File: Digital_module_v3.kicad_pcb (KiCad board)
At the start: 4 copper layers, 58.3 x 67.8 mm, 2 parts, among them J1 Pow_mng_iface, J7 Pow_mng_pow

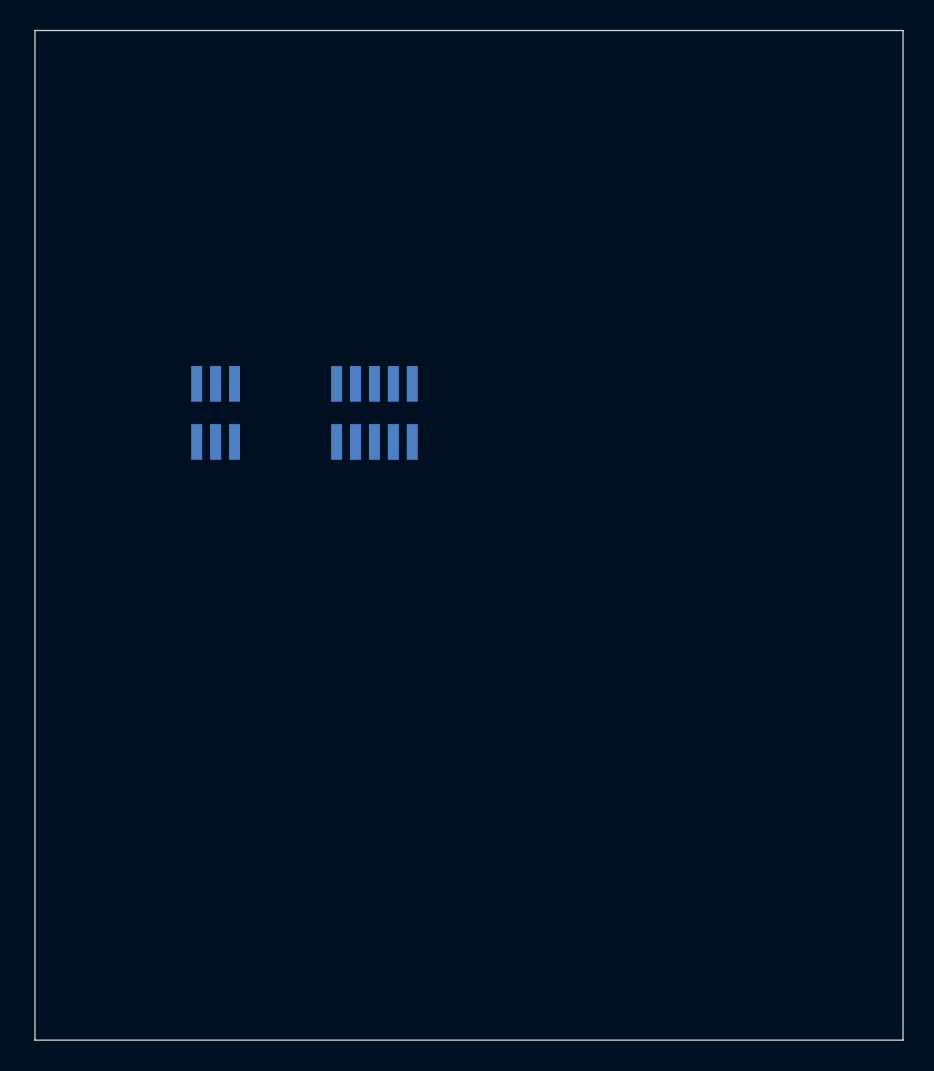
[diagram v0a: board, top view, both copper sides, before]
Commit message: Завершена трассировка печатной платы. Исправлены ошибки в схема.
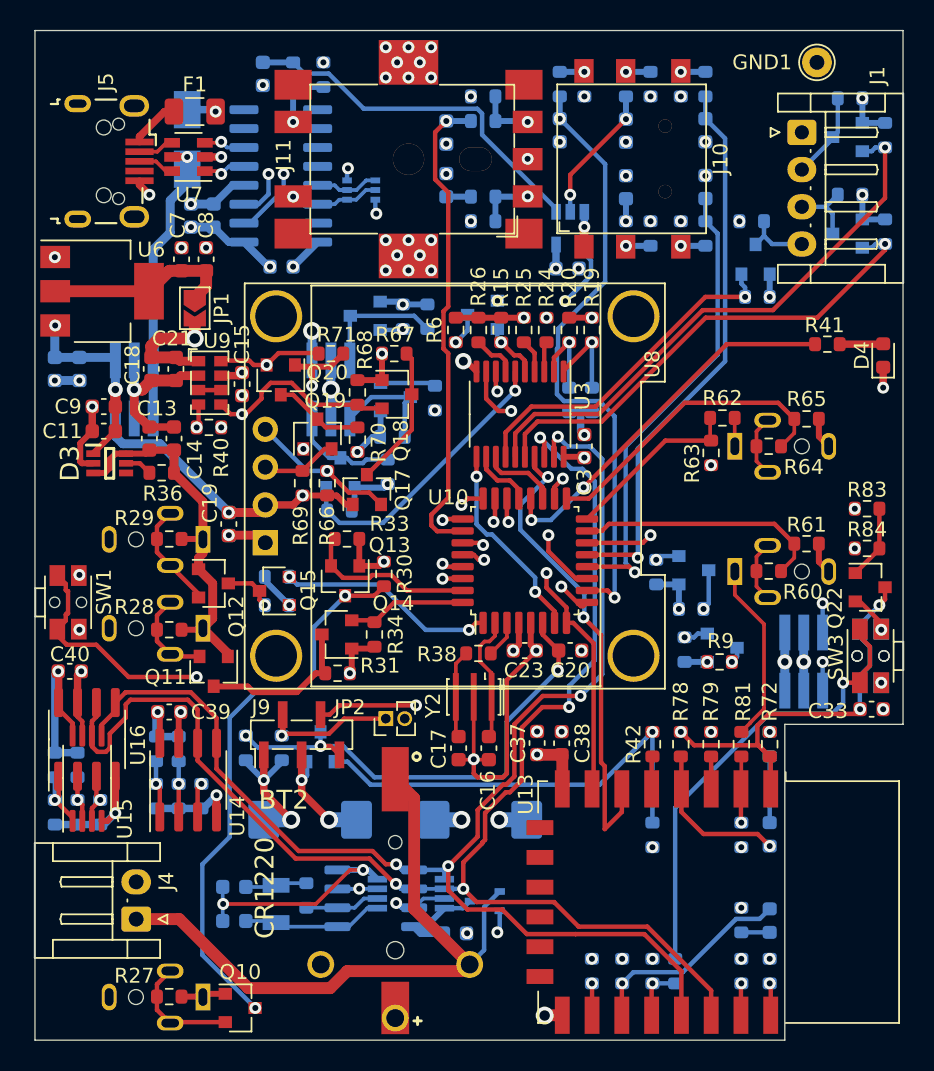
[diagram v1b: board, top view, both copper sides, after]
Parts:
- added BT1: CR2032, Modules:CR2032BS51, B.Cu at (100.0, 137.7)
- added BT2: CR1220, Modules:CR1220HSMD, F.Cu at (95.0, 133.0)
- added C1: 10pF, Capacitor_SMD:C_0603_1608Metric, B.Cu at (84.2, 134.8)
- added C10: 470uF, Capacitor_Tantalum_SMD:CP_EIA-7343-31_Kemet-D, B.Cu at (89.3, 128.0)
- added C11: 100nF, Capacitor_SMD:C_0603_1608Metric, F.Cu at (75.5, 101.9)
- added C12: 470uF, Capacitor_Tantalum_SMD:CP_EIA-7343-31_Kemet-D, B.Cu at (100.8, 128.0)
- added C13: 100nF, Capacitor_SMD:C_0603_1608Metric, F.Cu at (78.5, 102.4)
- added C14: 10uF, Capacitor_SMD:C_0603_1608Metric, F.Cu at (80.2, 102.4)
- added C15: 2.2uF, Capacitor_SMD:C_0603_1608Metric, F.Cu at (84.8, 98.7)
- added C16: 10pF, Capacitor_SMD:C_0603_1608Metric, F.Cu at (101.3, 123.2)
- added C17: 10pF, Capacitor_SMD:C_0603_1608Metric, F.Cu at (99.3, 123.2)
- added C18: 1.0uF, Capacitor_SMD:C_0603_1608Metric, F.Cu at (78.7, 97.7)
- added C19: 100nF, Capacitor_SMD:C_0603_1608Metric, F.Cu at (83.9, 108.1)
- added C2: 10pF, Capacitor_SMD:C_0603_1608Metric, B.Cu at (84.2, 132.5)
- added C20: 100nF, Capacitor_SMD:C_0603_1608Metric, F.Cu at (106.8, 116.6)
- added C21: 0.1uF, Capacitor_SMD:C_0603_1608Metric, F.Cu at (80.3, 97.7)
- added C22: 10uF, Capacitor_SMD:C_0603_1608Metric, B.Cu at (83.9, 108.1)
- added C23: 100nF, Capacitor_SMD:C_0603_1608Metric, F.Cu at (103.7, 116.6)
- added C24: 100nF, Capacitor_SMD:C_0603_1608Metric, B.Cu at (115.9, 85.5)
- added C25: 100nF, Capacitor_SMD:C_0603_1608Metric, B.Cu at (110.5, 81.7)
- added C26: 100nF, Capacitor_SMD:C_0603_1608Metric, B.Cu at (115.9, 81.7)
- added C27: 100nF, Capacitor_SMD:C_0603_1608Metric, B.Cu at (106.1, 81.7)
- added C28: 100nF, Capacitor_SMD:C_0603_1608Metric, B.Cu at (110.5, 85.5)
- added C29: 100nF, Capacitor_SMD:C_0603_1608Metric, B.Cu at (106.6, 91.0)
- added C3: 100nF, Capacitor_SMD:C_0603_1608Metric, F.Cu at (107.7, 102.9)
- added C30: 100nF, Capacitor_SMD:C_0603_1608Metric, B.Cu at (98.5, 85.4)
- added C31: 100nF, Capacitor_SMD:C_0603_1608Metric, B.Cu at (98.5, 81.9)
- added C32: 100nF, Capacitor_SMD:C_0603_1608Metric, B.Cu at (86.2, 77.9)
- added C33: 100nF, Capacitor_SMD:C_0603_1608Metric, F.Cu at (127.0, 120.6)
- added C34: 100nF, Capacitor_SMD:C_0603_1608Metric, B.Cu at (82.9, 87.4)
- added C35: 10uF, Capacitor_SMD:C_0603_1608Metric, B.Cu at (81.3, 87.4)
- added C36: 100nF, Capacitor_SMD:C_0603_1608Metric, B.Cu at (87.4, 90.9)
- added C37: 10uF, Capacitor_SMD:C_0603_1608Metric, F.Cu at (104.6, 122.8)
- added C38: 100nF, Capacitor_SMD:C_0603_1608Metric, F.Cu at (106.2, 122.9)
- added C39: 100nF, Capacitor_SMD:C_0603_1608Metric, F.Cu at (79.9, 120.8)
- added C4: 100nF, Capacitor_SMD:C_0603_1608Metric, B.Cu at (99.1, 135.6)
- added C40: 100nF, Capacitor_SMD:C_0603_1608Metric, F.Cu at (73.2, 118.0)
- added C5: 10uF, Capacitor_SMD:C_0603_1608Metric, B.Cu at (73.8, 97.7)
- added C6: 100nF, Capacitor_SMD:C_0603_1608Metric, B.Cu at (72.2, 97.7)
- added C7: 100nF, Capacitor_SMD:C_0603_1608Metric, F.Cu at (80.7, 90.4)
- added C8: 10uF, Capacitor_SMD:C_0603_1608Metric, F.Cu at (82.3, 90.4)
- added C9: 10uF, Capacitor_SMD:C_0603_1608Metric, F.Cu at (75.5, 100.3)
- added D1: BAT54CW, Package_TO_SOT_SMD:SOT-323_SC-70, B.Cu at (101.1, 133.5)
- added D2: SS14, Diode_SMD:D_SMA, B.Cu at (81.1, 82.3)
- added D3: LM66100DCKR, Modules:SOP65P210X110-6N, F.Cu at (75.9, 104.1)
- added D4: LED, LED_SMD:LED_0603_1608Metric, F.Cu at (127.8, 96.8)
- added D5: LED, LED_SMD:LED_0603_1608Metric, B.Cu at (120.2, 129.0)
- added D6: LED, LED_SMD:LED_0603_1608Metric, B.Cu at (120.2, 134.8)
- added F1: 0.5A, Fuse:Fuse_1206_3216Metric, F.Cu at (81.6, 80.4)
- added GND1: GND1, TestPoint:TestPoint_THTPad_D2.0mm_Drill1.0mm, F.Cu at (123.4, 77.1)
- added J10: JoystickSwitch, Modules:JoystickSwitch, F.Cu at (110.9, 83.6)
- added J11: JoystickSwitch, Modules:EC11_SMD, F.Cu at (95.9, 83.6)
- added J2: AUB-33, Modules:AUB-33, B.Cu at (122.4, 111.3)
- added J3: AUB-33, Modules:AUB-33, B.Cu at (122.4, 102.9)
- added J4: B2B-EH-A, Connector_JST:JST_EH_S2B-EH_1x02_P2.50mm_Horizontal, F.Cu at (77.6, 134.7)
- added J5: USB_B_Micro, Modules:USB_Micro-B_Wuerth_629105150521, F.Cu at (75.7, 83.8)
- added J6: AUB-33, Modules:AUB-33, B.Cu at (77.6, 139.9)
- added J8: AUB-33, Modules:AUB-33, B.Cu at (77.6, 109.2)
- added J9: SWD(PLS5), Connector_PinSocket_1.27mm:PinSocket_1x05_P1.27mm_Vertical_SMD_Pin1Left, F.Cu at (88.8, 122.3)
- added JP1: 3V3_en, Jumper:SolderJumper-2_P1.3mm_Open_TrianglePad1.0x1.5mm, F.Cu at (81.6, 93.6)
- added JP2: BOOT0, Connector_PinHeader_1.27mm:PinHeader_1x02_P1.27mm_Vertical, F.Cu at (94.4, 121.2)
- added Q1: BSS138, Package_TO_SOT_SMD:SOT-23, B.Cu at (125.4, 82.2)
- added Q10: BSS138, Package_TO_SOT_SMD:SOT-23, F.Cu at (84.6, 140.6)
- added Q11: BSS138, Package_TO_SOT_SMD:SOT-23, F.Cu at (82.9, 118.0)
- added Q12: BSS138, Package_TO_SOT_SMD:SOT-23, F.Cu at (82.8, 112.1)
- added Q13: BSS138, Package_TO_SOT_SMD:SOT-23, F.Cu at (91.7, 112.0)
- added Q14: BSS138, Package_TO_SOT_SMD:SOT-23, F.Cu at (91.1, 115.6)
- added Q15: BSS138, Package_TO_SOT_SMD:SOT-23, F.Cu at (86.9, 112.6)
- added Q16: 2N5551S, Package_TO_SOT_SMD:SOT-23, B.Cu at (90.0, 123.1)
- added Q17: BSS138, Package_TO_SOT_SMD:SOT-23, F.Cu at (93.1, 105.8)
- added Q18: BSS138, Package_TO_SOT_SMD:SOT-23, F.Cu at (95.2, 99.4)
- added Q19: BSS138, Package_TO_SOT_SMD:SOT-23, F.Cu at (89.8, 102.1)
- added Q2: BSS138, Package_TO_SOT_SMD:SOT-23, B.Cu at (125.4, 88.6)
- added Q20: BSS138, Package_TO_SOT_SMD:SOT-23, F.Cu at (87.4, 98.5)
- added Q21: UMH3N, Package_TO_SOT_SMD:SOT-363_SC-70-6, B.Cu at (92.8, 85.7)
- added Q22: 2N5551S, Package_TO_SOT_SMD:SOT-23, F.Cu at (126.9, 112.4)
- added Q3: BSS138, Package_TO_SOT_SMD:SOT-23, B.Cu at (119.2, 90.4)
- added Q4: BSS138, Package_TO_SOT_SMD:SOT-23, B.Cu at (95.1, 99.6)
- added Q5: BSS138, Package_TO_SOT_SMD:SOT-23, B.Cu at (91.4, 104.7)
- added Q6: BSS138, Package_TO_SOT_SMD:SOT-23, B.Cu at (100.9, 94.1)
- added Q7: BSS138, Package_TO_SOT_SMD:SOT-23, B.Cu at (93.0, 94.2)
- added Q8: BSS138, Package_TO_SOT_SMD:SOT-23, B.Cu at (115.1, 111.2)
- added Q9: BSS138, Package_TO_SOT_SMD:SOT-23, B.Cu at (117.0, 116.4)
- added R1: 10G, Resistor_SMD:R_0603_1608Metric, B.Cu at (125.6, 79.6)
- added R10: 10k, Resistor_SMD:R_0603_1608Metric, B.Cu at (127.9, 82.0)
- added R11: 10k, Resistor_SMD:R_0603_1608Metric, B.Cu at (127.9, 88.5)
- added R12: 10k, Resistor_SMD:R_0603_1608Metric, B.Cu at (119.4, 92.9)
- added R13: 10k, Resistor_SMD:R_0603_1608Metric, B.Cu at (97.7, 99.7)
- added R14: 10k, Resistor_SMD:R_0603_1608Metric, B.Cu at (91.3, 107.2)
- added R15: 10k, Resistor_SMD:R_0603_1608Metric, F.Cu at (102.2, 95.1)
- added R16: 10k, Resistor_SMD:R_0603_1608Metric, B.Cu at (95.6, 94.2)
- added R17: 10k, Resistor_SMD:R_0603_1608Metric, B.Cu at (112.6, 111.4)
- added R18: 10k, Resistor_SMD:R_0603_1608Metric, B.Cu at (114.5, 116.6)
- added R19: 10k, Resistor_SMD:R_0603_1608Metric, F.Cu at (108.3, 95.1)
- added R2: 10G, Resistor_SMD:R_0603_1608Metric, B.Cu at (125.6, 86.0)
- added R20: 10k, Resistor_SMD:R_0603_1608Metric, F.Cu at (106.7, 95.1)
- added R21: 10k, Resistor_SMD:R_0603_1608Metric, B.Cu at (108.3, 99.8)
- added R22: 10k, Resistor_SMD:R_0603_1608Metric, B.Cu at (106.7, 99.8)
- added R23: 50, Resistor_SMD:R_0603_1608Metric, B.Cu at (89.1, 133.1)
- added R24: 10k, Resistor_SMD:R_0603_1608Metric, F.Cu at (105.2, 95.1)
- added R25: 10k, Resistor_SMD:R_0603_1608Metric, F.Cu at (103.7, 95.1)
- added R26: 10k, Resistor_SMD:R_0603_1608Metric, F.Cu at (100.6, 95.1)
- added R27: 10k, Resistor_SMD:R_0603_1608Metric, F.Cu at (79.9, 139.9)
- added R28: 10k, Resistor_SMD:R_0603_1608Metric, F.Cu at (79.9, 115.2)
- added R29: 10k, Resistor_SMD:R_0603_1608Metric, F.Cu at (79.9, 109.1)
- added R3: 10G, Resistor_SMD:R_0603_1608Metric, B.Cu at (119.0, 87.8)
- added R30: 10G, Resistor_SMD:R_0603_1608Metric, F.Cu at (94.3, 111.5)
- added R31: 10G, Resistor_SMD:R_0603_1608Metric, F.Cu at (91.2, 118.2)
- added R32: 10G, Resistor_SMD:R_0603_1608Metric, B.Cu at (87.1, 113.6)
- added R33: 10k, Resistor_SMD:R_0603_1608Metric, F.Cu at (91.8, 109.1)
- added R34: 10k, Resistor_SMD:R_0603_1608Metric, F.Cu at (93.6, 115.6)
- added R35: 10k, Resistor_SMD:R_0603_1608Metric, B.Cu at (87.1, 111.7)
- added R36: 10k, Resistor_SMD:R_0603_1608Metric, F.Cu at (79.4, 104.7)
- added R37: 10k, Resistor_SMD:R_0603_1608Metric, B.Cu at (87.4, 123.2)
- added R38: 50, Resistor_SMD:R_0603_1608Metric, F.Cu at (100.6, 116.8)
- added R39: 10k, Resistor_SMD:R_0603_1608Metric, B.Cu at (85.0, 123.2)
- added R4: 2.2M, Resistor_SMD:R_0603_1608Metric, B.Cu at (94.9, 102.3)
- added R40: 10k, Resistor_SMD:R_0603_1608Metric, F.Cu at (82.5, 101.7)
- added R41: 1k, Resistor_SMD:R_0603_1608Metric, F.Cu at (124.1, 96.1)
- added R42: 10k, Resistor_SMD:R_0603_1608Metric, F.Cu at (112.3, 122.9)
- added R43: 10k, Resistor_SMD:R_0603_1608Metric, B.Cu at (112.3, 129.0)
- added R44: 100k, Resistor_SMD:R_0603_1608Metric, B.Cu at (114.2, 88.6)
- added R45: 100k, Resistor_SMD:R_0603_1608Metric, B.Cu at (112.2, 78.6)
- added R46: 100k, Resistor_SMD:R_0603_1608Metric, B.Cu at (114.2, 78.6)
- added R47: 100k, Resistor_SMD:R_0603_1608Metric, B.Cu at (107.7, 78.6)
- added R48: 100k, Resistor_SMD:R_0603_1608Metric, B.Cu at (112.2, 88.6)
- added R49: 10k, Resistor_SMD:R_0603_1608Metric, B.Cu at (115.9, 88.6)
- added R5: 2.2M, Resistor_SMD:R_0603_1608Metric, B.Cu at (94.5, 104.6)
- added R50: 10k, Resistor_SMD:R_0603_1608Metric, B.Cu at (110.5, 78.6)
- added R51: 10k, Resistor_SMD:R_0603_1608Metric, B.Cu at (115.9, 78.6)
- added R52: 10k, Resistor_SMD:R_0603_1608Metric, B.Cu at (106.1, 78.6)
- added R53: 10k, Resistor_SMD:R_0603_1608Metric, B.Cu at (110.5, 88.6)
- added R54: 100k, Resistor_SMD:R_0603_1608Metric, B.Cu at (101.0, 87.8)
- added R55: 100k, Resistor_SMD:R_0603_1608Metric, B.Cu at (101.0, 79.4)
- added R56: 100k, Resistor_SMD:R_0603_1608Metric, B.Cu at (90.2, 78.0)
- added R57: 10k, Resistor_SMD:R_0603_1608Metric, B.Cu at (101.0, 86.2)
- added R58: 10k, Resistor_SMD:R_0603_1608Metric, B.Cu at (101.0, 81.1)
- added R59: 10k, Resistor_SMD:R_0603_1608Metric, B.Cu at (88.2, 78.0)
- added R6: 2.2M, Resistor_SMD:R_0603_1608Metric, F.Cu at (99.1, 95.1)
- added R60: 220k, Resistor_SMD:R_0603_1608Metric, F.Cu at (120.1, 111.3)
- added R61: 100k, Resistor_SMD:R_0603_1608Metric, F.Cu at (122.7, 109.5)
- added R62: 220k, Resistor_SMD:R_0603_1608Metric, F.Cu at (117.0, 101.0)
- added R63: 100k, Resistor_SMD:R_0603_1608Metric, F.Cu at (116.3, 103.4)
- added R64: 220k, Resistor_SMD:R_0603_1608Metric, F.Cu at (120.1, 102.9)
- added R65: 100k, Resistor_SMD:R_0603_1608Metric, F.Cu at (122.7, 101.1)
- added R66: 10k, Resistor_SMD:R_0603_1608Metric, F.Cu at (90.5, 105.4)
- added R67: 1M, Resistor_SMD:R_0603_1608Metric, F.Cu at (95.0, 96.7)
- added R68: 10k, Resistor_SMD:R_0603_1608Metric, F.Cu at (92.5, 99.3)
- added R69: 10k, Resistor_SMD:R_0603_1608Metric, F.Cu at (88.8, 105.4)
- added R7: 2.2M, Resistor_SMD:R_0603_1608Metric, B.Cu at (97.2, 94.2)
- added R70: 1M, Resistor_SMD:R_0603_1608Metric, F.Cu at (92.5, 102.5)
- added R71: 10k, Resistor_SMD:R_0603_1608Metric, F.Cu at (90.7, 96.7)
- added R72: 10k, Resistor_SMD:R_0603_1608Metric, F.Cu at (120.2, 122.9)
- added R73: 1k, Resistor_SMD:R_0603_1608Metric, B.Cu at (120.2, 122.9)
- added R74: 10k, Resistor_SMD:R_0603_1608Metric, B.Cu at (112.3, 138.2)
- added R75: 10k, Resistor_SMD:R_0603_1608Metric, B.Cu at (110.3, 138.2)
- added R76: 1k, Resistor_SMD:R_0603_1608Metric, B.Cu at (118.3, 134.7)
- added R77: 470, Resistor_SMD:R_0603_1608Metric, B.Cu at (113.8, 138.2)
- added R78: 470, Resistor_SMD:R_0603_1608Metric, F.Cu at (114.2, 122.9)
- added R79: 10k, Resistor_SMD:R_0603_1608Metric, F.Cu at (116.3, 122.9)
- added R8: 10G, Resistor_SMD:R_0603_1608Metric, B.Cu at (114.9, 113.8)
- added R80: 10k, Resistor_SMD:R_0603_1608Metric, B.Cu at (108.3, 138.2)
- added R81: 220k, Resistor_SMD:R_0603_1608Metric, F.Cu at (118.3, 122.9)
- added R82: 100k, Resistor_SMD:R_0603_1608Metric, B.Cu at (118.3, 129.0)
- added R83: 10k, Resistor_SMD:R_0603_1608Metric, F.Cu at (126.7, 107.1)
- added R84: 10k, Resistor_SMD:R_0603_1608Metric, F.Cu at (126.7, 109.8)
- added R85: 470, Resistor_SMD:R_0603_1608Metric, B.Cu at (118.3, 138.2)
- added R86: 470, Resistor_SMD:R_0603_1608Metric, B.Cu at (120.2, 138.2)
- added R87: 10k, Resistor_SMD:R_0603_1608Metric, B.Cu at (72.2, 124.3)
- added R88: 10k, Resistor_SMD:R_0603_1608Metric, B.Cu at (73.7, 124.3)
- added R89: 10k, Resistor_SMD:R_0603_1608Metric, B.Cu at (79.0, 123.2)
- added R9: 10G, Resistor_SMD:R_0603_1608Metric, F.Cu at (116.8, 117.4)
- added R90: 10k, Resistor_SMD:R_0603_1608Metric, B.Cu at (80.5, 123.2)
- added R91: 10k, Resistor_SMD:R_0603_1608Metric, B.Cu at (72.2, 127.5)
- added R92: 10k, Resistor_SMD:R_0603_1608Metric, B.Cu at (73.7, 127.5)
- added R93: 10k, Resistor_SMD:R_0603_1608Metric, B.Cu at (79.0, 126.4)
- added R94: 10k, Resistor_SMD:R_0603_1608Metric, B.Cu at (80.5, 126.4)
- added R95: 10k, Resistor_SMD:R_0603_1608Metric, B.Cu at (82.0, 126.4)
- added R96: 10k, Resistor_SMD:R_0603_1608Metric, B.Cu at (75.2, 127.5)
- added SW1: SW_Rst, Modules:SW_SPST_EVQP7C, F.Cu at (73.1, 113.4)
- added SW2: SW_RST, Modules:SW_SPST_EVQP7C, B.Cu at (127.0, 117.0)
- added SW3: SW_FLASH, Modules:SW_SPST_EVQP7C, F.Cu at (127.0, 117.0)
- added U1: Power_manager_2_v3_wo3D, Modules:Power_manager_2_v3_wo3D, B.Cu at (100.0, 96.0)
- added U10: STM32G030K6Tx, Package_QFP:LQFP-32_7x7mm_P0.8mm, F.Cu at (103.7, 110.6)
- added U11: SN74LVC1G08DBVR, Package_TO_SOT_SMD:SOT-23-5, B.Cu at (106.8, 88.3)
- added U12: CH340C, Package_SO:SOIC-16_3.9x9.9mm_P1.27mm, B.Cu at (87.4, 84.8)
- added U13: ESP-12F, RF_Module:ESP-12E, F.Cu at (116.8, 133.5)
- added U14: FM24C64B, Package_SO:SOIC-8_3.9x4.9mm_P1.27mm, F.Cu at (81.1, 125.3)
- added U15: AT24CS64-XHM, Package_SO:TSSOP-8_4.4x3mm_P0.65mm, F.Cu at (74.4, 125.2)
- added U16: AT24CS64-SSHM, Package_SO:SOIC-8_3.9x4.9mm_P1.27mm, F.Cu at (74.3, 122.6)
- added U2: Fan_control_module_2_v3, Modules:Fan_controller_2_v3_wo3D, B.Cu at (100.0, 120.5)
- added U3: PCA9544APW, Package_SO:TSSOP-20_4.4x6.5mm_P0.65mm, F.Cu at (103.4, 100.8)
- added U4: PCF8563TS, Modules:SOT65P490X110-8N, B.Cu at (96.1, 133.0)
- added U5: PCF8563TS, Package_SO:SO-8_3.9x4.9mm_P1.27mm, B.Cu at (93.7, 133.3)
- added U6: LM1117-3.3, Package_TO_SOT_SMD:SOT-223-3_TabPin2, F.Cu at (75.4, 92.5)
- added U7: USBLC6-2SC6, Package_TO_SOT_SMD:SOT-23-6, F.Cu at (81.2, 83.5)
- added U8: SSD1306, Modules:SSD1306_2_I2C, F.Cu at (86.3, 109.4)
- added U9: AP3216C, Modules:AP3216C, F.Cu at (81.8, 97.2)
- added Y1: SC-32S 32.768KHz, Crystal:Crystal_SMD_3215-2Pin_3.2x1.5mm, B.Cu at (87.0, 133.7)
- added Y2: CSTCE8M, Crystal:Resonator_SMD_muRata_CSTxExxV-3Pin_3.0x1.1mm_HandSoldering, F.Cu at (100.3, 119.7)
- J1: value Pow_mng_iface -> B2B-EH-A; footprint Connector_PinHeader_1.27mm:PinHeader_2x05_P1.27mm_Vertical_SMD -> Connector_JST:JST_EH_S4B-EH_1x04_P2.50mm_Horizontal; moved to F.Cu
- J7: value Pow_mng_pow -> AUB-33; footprint Connector_PinHeader_1.27mm:PinHeader_2x03_P1.27mm_Vertical_SMD -> Modules:AUB-33
- moved J1 34.3 mm to (122.4, 81.8), turned to 270 degrees
- moved J7 15.4 mm to (77.6, 115.1), turned to 0 degrees
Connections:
- J1 pad 2: GND1 -> /sda1
- J1 pad 3: /+5V_st -> /scl1
- J1 pad 4: /+5V_st -> Net-(J1-Pad4)
- J7 pad 1: +5VP -> +5VD
- J7 pad 2: +5VP -> GND1
- J7 pad 3: GND1 -> Net-(J7-Pad3)
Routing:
- net GND1: track 0.00 -> 122.4 mm, vias 0 -> 57
- net +3V3: track 0.00 -> 107.8 mm, vias 0 -> 47
- net /I2C_SCL: track 0.00 -> 97.6 mm, vias 0 -> 4
- net /I2C_SDA: track 0.00 -> 93.7 mm, vias 0 -> 4
- net +5P: track 0.00 -> 82.1 mm, vias 0 -> 6
- net Net-(R86-Pad2): track 0.00 -> 79.1 mm, vias 0 -> 2
- net Net-(R85-Pad2): track 0.00 -> 77.9 mm, vias 0 -> 2
- net /ESP32_part/~RST: track 0.00 -> 73.1 mm, vias 0 -> 4
- net /ESP32_part/GPIO0: track 0.00 -> 67.7 mm, vias 0 -> 2
- net +5VD: track 0.00 -> 54.7 mm
- net /Ctrl_part/~RST: track 0.00 -> 54.1 mm, vias 0 -> 4
- net /ESP_LED: track 0.00 -> 48.0 mm, vias 0 -> 2
- net Net-(BT1-Pad1): track 0.00 -> 45.2 mm
- net /Ctrl_part/jlline: track 0.00 -> 41.3 mm, vias 0 -> 2
- net /Ctrl_part/jcline: track 0.00 -> 41.2 mm, vias 0 -> 3
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- added copper zone on In1.Cu, net +3V3
- added copper zone on In2.Cu, net GND1
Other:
- outline, holes or cut-outs redrawn

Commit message: Добавлен BOM-файл в HTML-формате, гербера и файлы сверловки
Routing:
- net Net-(R86-Pad2): track 79.1 -> 83.1 mm
- net Net-(R85-Pad2): track 77.9 -> 81.9 mm
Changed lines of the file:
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@@
     (thickness 1.6)
     (drawings 33)
-    (tracks 1413)
+    (tracks 1420)
     (zones 0)
     (modules 202)
@@
       (effects (font (size 1 1) (thickness 0.15)) (justify mirror))
     )
-    (fp_text user %R (at 0 -10.16 -180) (layer B.Fab)
-      (effects (font (size 1 1) (thickness 0.15)) (justify mirror))
-    )
     (fp_line (start 21.082 -4.572) (end 20.447 -3.937) (layer B.Fab) (width 0.1))
     (fp_line (start 20.447 -1.651) (end 20.447 -3.937) (layer B.Fab) (width 0.1))
@@
     (fp_line (start 20.32 -6.35) (end 20.32 -1.6) (layer B.CrtYd) (width 0.12))
     (fp_line (start 25 -6.35) (end 20.32 -6.35) (layer B.CrtYd) (width 0.12))
+    (fp_text user %R (at 0 -10.16 -180) (layer B.Fab)
+      (effects (font (size 1 1) (thickness 0.15)) (justify mirror))
+    )
     (pad 2.3 smd rect (at 22.479 -5.05) (size 0.74 2.4) (layers B.Cu B.Paste B.Mask)
       (net 1 GND1))
@@
       (effects (font (size 1 1) (thickness 0.15)) (justify mirror))
     )
-    (pad 2 smd roundrect (at 3.1125 0) (size 2.075 2.55) (layers B.Cu B.Paste B.Mask) (roundrect_rratio 0.120482)
+    (pad 2 smd roundrect (at 3.1125 0) (size 2.075 2.55) (layers B.Cu B.Paste B.Mask) (roundrect_rratio 0.1204819277108434)
       (net 1 GND1))
-    (pad 1 smd roundrect (at -3.1125 0) (size 2.075 2.55) (layers B.Cu B.Paste B.Mask) (roundrect_rratio 0.120482)
+    (pad 1 smd roundrect (at -3.1125 0) (size 2.075 2.55) (layers B.Cu B.Paste B.Mask) (roundrect_rratio 0.1204819277108434)
       (net 5 +3V3))
     (model ${KISYS3DMOD}/Capacitor_Tantalum_SMD.3dshapes/CP_EIA-7343-31_Kemet-D.wrl
@@
       (effects (font (size 1 1) (thickness 0.15)) (justify mirror))
     )
-    (pad 2 smd roundrect (at 3.1125 0 180) (size 2.075 2.55) (layers B.Cu B.Paste B.Mask) (roundrect_rratio 0.120482)
+    (pad 2 smd roundrect (at 3.1125 0 180) (size 2.075 2.55) (layers B.Cu B.Paste B.Mask) (roundrect_rratio 0.1204819277108434)
       (net 1 GND1))
-    (pad 1 smd roundrect (at -3.1125 0 180) (size 2.075 2.55) (layers B.Cu B.Paste B.Mask) (roundrect_rratio 0.120482)
+    (pad 1 smd roundrect (at -3.1125 0 180) (size 2.075 2.55) (layers B.Cu B.Paste B.Mask) (roundrect_rratio 0.1204819277108434)
       (net 5 +3V3))
     (model ${KISYS3DMOD}/Capacitor_Tantalum_SMD.3dshapes/CP_EIA-7343-31_Kemet-D.wrl
@@
     (pad 2 thru_hole oval (at 2.5 0 270) (size 1.7 1.95) (drill 0.95) (layers *.Cu *.Mask)
       (net 55 /sda1))
-    (pad 1 thru_hole roundrect (at 0 0 270) (size 1.7 1.95) (drill 0.95) (layers *.Cu *.Mask) (roundrect_rratio 0.147059)
+    (pad 1 thru_hole roundrect (at 0 0 270) (size 1.7 1.95) (drill 0.95) (layers *.Cu *.Mask) (roundrect_rratio 0.1470588235294118)
       (net 1 GND1))
     (model ${KISYS3DMOD}/Connector_JST.3dshapes/JST_EH_S4B-EH_1x04_P2.50mm_Horizontal.wrl
@@
     (pad 2 thru_hole oval (at 2.5 0 90) (size 1.7 2) (drill 1) (layers *.Cu *.Mask)
       (net 1 GND1))
-    (pad 1 thru_hole roundrect (at 0 0 90) (size 1.7 2) (drill 1) (layers *.Cu *.Mask) (roundrect_rratio 0.147059)
+    (pad 1 thru_hole roundrect (at 0 0 90) (size 1.7 2) (drill 1) (layers *.Cu *.Mask) (roundrect_rratio 0.1470588235294118)
       (net 4 "Net-(BT1-Pad1)"))
     (model ${KISYS3DMOD}/Connector_JST.3dshapes/JST_EH_S2B-EH_1x02_P2.50mm_Horizontal.wrl
@@
   (segment (start 85.298924 87.9348) (end 87.5538 85.679924) (width 0.3) (layer B.Cu) (net 67))
   (segment (start 84.8868 87.9348) (end 85.298924 87.9348) (width 0.3) (layer B.Cu) (net 67))
-  (segment (start 92.93382 113.09382) (end 117.1778 137.3378) (width 0.3) (layer In2.Cu) (net 67))
-  (segment (start 88.17379 106.79679) (end 88.17379 107.626658) (width 0.3) (layer In2.Cu) (net 67))
+  (segment (start 117.1778 137.3378) (end 118.2878 137.3378) (width 0.3) (layer In2.Cu) (net 67))
+  (segment (start 106.3398 126.4998) (end 117.1778 137.3378) (width 0.3) (layer In2.Cu) (net 67))
+  (segment (start 97.816249 124.816249) (end 99.4998 126.4998) (width 0.3) (layer In2.Cu) (net 67))
   (segment (start 92.93382 112.386688) (end 92.93382 113.09382) (width 0.3) (layer In2.Cu) (net 67))
-  (segment (start 86.894801 105.517801) (end 88.17379 106.79679) (width 0.3) (layer In2.Cu) (net 67))
+  (segment (start 87.5538 85.212922) (end 83.9978 88.768922) (width 0.3) (layer In2.Cu) (net 67))
+  (segment (start 83.9978 88.768922) (end 83.9978 97.3328) (width 0.3) (layer In2.Cu) (net 67))
+  (segment (start 83.9978 97.3328) (end 80.961799 100.368801) (width 0.3) (layer In2.Cu) (net 67))
+  (segment (start 80.961799 100.368801) (end 80.961799 102.551799) (width 0.3) (layer In2.Cu) (net 67))
+  (segment (start 99.4998 126.4998) (end 106.3398 126.4998) (width 0.3) (layer In2.Cu) (net 67))
+  (segment (start 80.961799 102.551799) (end 83.927801 105.517801) (width 0.3) (layer In2.Cu) (net 67))
   (segment (start 83.927801 105.517801) (end 86.894801 105.517801) (width 0.3) (layer In2.Cu) (net 67))
+  (segment (start 86.894801 105.517801) (end 88.17379 106.79679) (width 0.3) (layer In2.Cu) (net 67))
+  (segment (start 88.17379 106.79679) (end 88.17379 107.626658) (width 0.3) (layer In2.Cu) (net 67))
   (segment (start 88.17379 107.626658) (end 92.93382 112.386688) (width 0.3) (layer In2.Cu) (net 67))
-  (segment (start 80.961799 102.551799) (end 83.927801 105.517801) (width 0.3) (layer In2.Cu) (net 67))
-  (segment (start 80.961799 100.368801) (end 80.961799 102.551799) (width 0.3) (layer In2.Cu) (net 67))
-  (segment (start 83.9978 97.3328) (end 80.961799 100.368801) (width 0.3) (layer In2.Cu) (net 67))
-  (segment (start 83.9978 88.768922) (end 83.9978 97.3328) (width 0.3) (layer In2.Cu) (net 67))
-  (segment (start 117.1778 137.3378) (end 118.2878 137.3378) (width 0.3) (layer In2.Cu) (net 67))
-  (segment (start 87.5538 85.212922) (end 83.9978 88.768922) (width 0.3) (layer In2.Cu) (net 67))
+  (segment (start 92.93382 113.09382) (end 97.816249 117.976251) (width 0.3) (layer In2.Cu) (net 67))
   (segment (start 87.5538 84.6328) (end 87.5538 85.212922) (width 0.3) (layer In2.Cu) (net 67))
+  (segment (start 97.816249 117.976251) (end 97.816249 124.816249) (width 0.3) (layer In2.Cu) (net 67))
   (via (at 120.1928 137.3378) (size 0.8) (drill 0.4) (layers F.Cu B.Cu) (net 68))
   (segment (start 86.5378 85.9888) (end 86.5378 84.6328) (width 0.3) (layer B.Cu) (net 68))
@@
   (segment (start 84.8868 86.6648) (end 85.8618 86.6648) (width 0.3) (layer B.Cu) (net 68))
   (via (at 86.5378 84.6328) (size 0.8) (drill 0.4) (layers F.Cu B.Cu) (net 68))
-  (segment (start 86.5378 85.5218) (end 83.497789 88.561811) (width 0.3) (layer In2.Cu) (net 68))
-  (segment (start 86.5378 84.6328) (end 86.5378 85.5218) (width 0.3) (layer In2.Cu) (net 68))
+  (segment (start 119.442799 138.087801) (end 120.1928 137.3378) (width 0.3) (layer In2.Cu) (net 68))
   (segment (start 117.220679 138.087801) (end 119.442799 138.087801) (width 0.3) (layer In2.Cu) (net 68))
-  (segment (start 83.497789 88.561811) (end 83.497789 97.125689) (width 0.3) (layer In2.Cu) (net 68))
+  (segment (start 106.132689 126.999811) (end 117.220679 138.087801) (width 0.3) (layer In2.Cu) (net 68))
+  (segment (start 99.292689 126.999811) (end 106.132689 126.999811) (width 0.3) (layer In2.Cu) (net 68))
+  (segment (start 86.5378 84.6328) (end 83.497789 87.672811) (width 0.3) (layer In2.Cu) (net 68))
+  (segment (start 97.316239 125.023361) (end 99.292689 126.999811) (width 0.3) (layer In2.Cu) (net 68))
+  (segment (start 83.497789 87.672811) (end 83.497789 97.125689) (width 0.3) (layer In2.Cu) (net 68))
+  (segment (start 83.497789 97.125689) (end 80.4418 100.181678) (width 0.3) (layer In2.Cu) (net 68))
   (segment (start 80.4418 100.181678) (end 80.4418 102.775301) (width 0.3) (layer In2.Cu) (net 68))
   (segment (start 80.4418 102.775301) (end 85.864298 108.197799) (width 0.3) (layer In2.Cu) (net 68))
@@
   (segment (start 87.330677 108.197799) (end 91.336677 112.203799) (width 0.3) (layer In2.Cu) (net 68))
   (segment (start 91.336677 112.203799) (end 92.043809 112.203799) (width 0.3) (layer In2.Cu) (net 68))
-  (segment (start 83.497789 97.125689) (end 80.4418 100.181678) (width 0.3) (layer In2.Cu) (net 68))
   (segment (start 92.043809 112.203799) (end 92.433809 112.593799) (width 0.3) (layer In2.Cu) (net 68))
-  (segment (start 119.442799 138.087801) (end 120.1928 137.3378) (width 0.3) (layer In2.Cu) (net 68))
-  (segment (start 92.433809 112.593799) (end 92.433809 113.300931) (width 0.3) (layer In2.Cu) (net 68))
-  (segment (start 92.433809 113.300931) (end 117.220679 138.087801) (width 0.3) (layer In2.Cu) (net 68))
+  (segment (start 92.433809 112.593799) (end 92.43381 113.300932) (width 0.3) (layer In2.Cu) (net 68))
+  (segment (start 92.43381 113.300932) (end 97.316239 118.183361) (width 0.3) (layer In2.Cu) (net 68))
+  (segment (start 97.316239 118.183361) (end 97.316239 125.023361) (width 0.3) (layer In2.Cu) (net 68))
   (via (at 83.362804 82.4738) (size 0.8) (drill 0.4) (layers F.Cu B.Cu) (net 69) (status 40000))
   (segment (start 83.296804 82.5398) (end 83.362804 82.4738) (width 0.25) (layer F.Cu) (net 69) (status 40000))
